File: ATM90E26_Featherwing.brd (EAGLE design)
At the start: 49.9 x 39.4 mm, 56 parts, among them J1 ST-PJ-312, J2 4P-SMD-2.0-90D, J3 4P-SMD-2.0-90D, J4 12V AC, Q1 8.192MHz, U1 ATM90E26, U2 CJT1117-5.0-SOT223

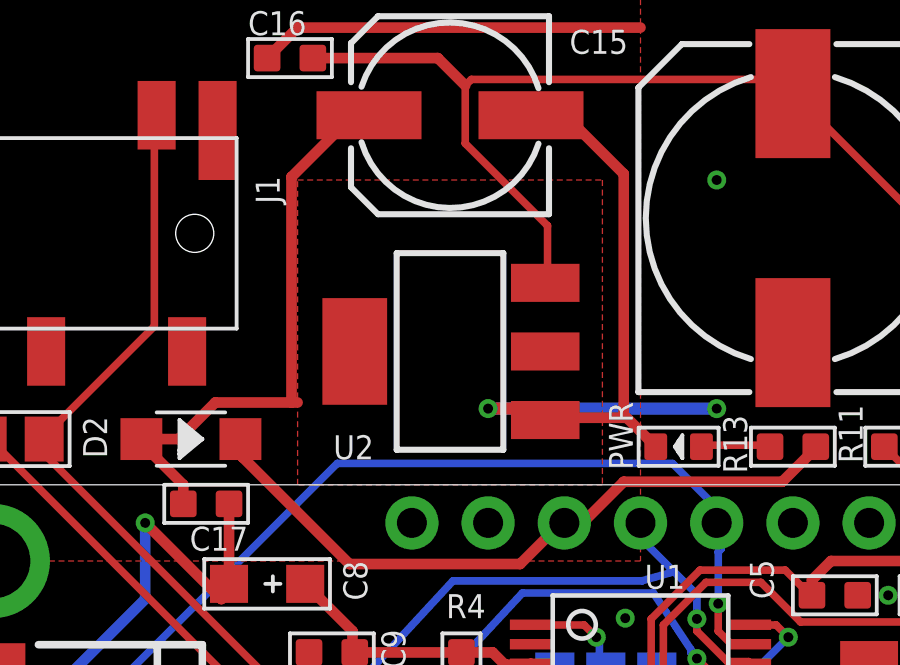
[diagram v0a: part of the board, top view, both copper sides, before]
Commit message: Added thermal pad and fixed silk screen
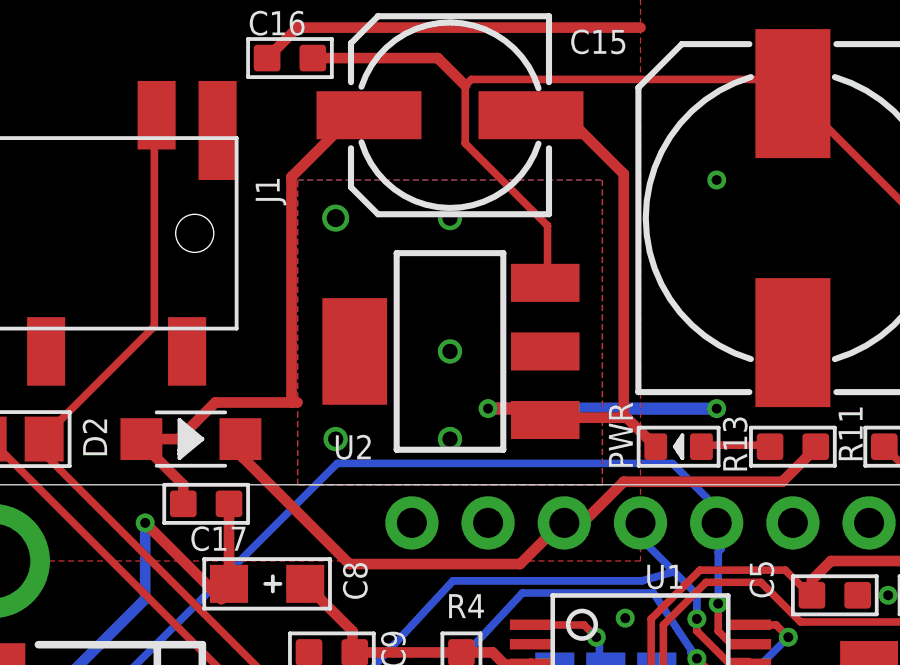
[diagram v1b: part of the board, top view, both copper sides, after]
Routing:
- net V_OUT: vias 0 -> 5
- added copper zone on layer 16, net V_OUT
